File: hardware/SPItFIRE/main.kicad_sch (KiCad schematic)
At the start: 36 parts, among them J1 Compact Host, J10 ISP, J11 Joystick A, J12 Joystick B, J13 Peripheral DE-9, J14 Peripheral User Port, J2 User Port Host, J3 User Port Passthrough, J4 SD Card Adapter, J5 DeadOnRTC, J6 SPI_4, J7 SPI_5, J8 SPI_6, J9 SPI_7, U1 74HC138, U2 ATmega1284P-A, Y1 Crystal

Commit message: Work in progress on layout and routing
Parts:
- C1, C10, C4, C5, C7, C8, C9, R1, R2, R3, R4, R5, R6: footprint (none) -> Capacitor_SMD:C_0603_1608Metric_Pad1.08x0.95mm_HandSolder
- C2, C6: footprint (none) -> Capacitor_SMD:C_0201_0603Metric_Pad0.64x0.40mm_HandSolder
- C3, D2: footprint (none) -> LED_SMD:LED_0603_1608Metric_Pad1.05x0.95mm_HandSolder
- D1: footprint (none) -> Diode_SMD:D_SOD-123
- J10: footprint Package_SO:SOIC-16_3.9x9.9mm_P1.27mm -> Connector_IDC:IDC-Header_2x03_P2.54mm_Vertical
- J14, J2: footprint Connector_PinHeader_2.54mm:PinHeader_2x10_P2.54mm_Horizontal -> Connector_IDC:IDC-Header_2x10_P2.54mm_Latch_Horizontal
- J3: footprint Connector_PinHeader_2.54mm:PinHeader_2x10_P2.54mm_Vertical -> Connector_IDC:IDC-Header_2x10_P2.54mm_Vertical
- L1: footprint (none) -> Inductor_SMD:L_0805_2012Metric_Pad1.05x1.20mm_HandSolder
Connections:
- net AGND is gone; now on net GND: J11.8, J12.8
- net VREF is gone; now on net AVCC: J11.11 (P111), J11.14 (P14), J12.11 (P111), J12.14 (P14)
- net AVCC: now reaches C9.1, L1.2, U2.27 (AVCC)
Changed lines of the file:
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@@
 	)
 	(junction
+		(at 275.59 236.22)
+		(diameter 0)
+		(color 0 0 0 0)
+	)
+	(junction
 		(at 219.71 270.51)
 		(diameter 0)
@@
 	(wire
 		(pts
+			(xy 275.59 236.22) (xy 287.02 236.22)
+		)
+		(stroke
+			(width 0)
+			(type default)
+		)
+	)
+	(wire
+		(pts
 			(xy 284.48 252.73) (xy 287.02 252.73)
 		)
@@
 		)
 	)
+	(label "AVCC"
+		(at 363.22 64.77 0)
+		(effects
+			(font
+				(size 1.27 1.27)
+			)
+			(justify left bottom)
+		)
+	)
 	(global_label "PD2"
 		(shape bidirectional)
@@
 		)
 	)
-	(global_label "VREF"
+	(global_label "AVCC"
 		(shape passive)
 		(at 363.22 114.3 180)
@@
 		)
 		(property "Intersheetrefs" "${INTERSHEET_REFS}"
-			(at 356.7499 114.3 0)
+			(at 356.6289 114.3 0)
 			(hide yes)
 			(show_name no)
@@
 		)
 	)
-	(global_label "VREF"
+	(global_label "AVCC"
 		(shape passive)
 		(at 363.22 129.54 180)
@@
 		)
 		(property "Intersheetrefs" "${INTERSHEET_REFS}"
-			(at 356.7499 129.54 0)
+			(at 356.6289 129.54 0)
 			(hide yes)
 			(show_name no)
@@
 		)
 	)
+	(global_label "AVCC"
+		(shape passive)
+		(at 287.02 236.22 0)
+		(fields_autoplaced yes)
+		(effects
+			(font
+				(size 1.27 1.27)
+			)
+			(justify left)
+		)
+		(property "Intersheetrefs" "${INTERSHEET_REFS}"
+			(at 293.6111 236.22 0)
+			(hide yes)
+			(show_name no)
+			(do_not_autoplace no)
+			(effects
+				(font
+					(size 1.27 1.27)
+				)
+				(justify left)
+			)
+		)
+	)
 	(global_label "PC1"
 		(shape bidirectional)
@@
 		)
 	)
-	(global_label "VREF"
+	(global_label "AVCC"
 		(shape passive)
 		(at 363.22 64.77 180)
@@
 		)
 		(property "Intersheetrefs" "${INTERSHEET_REFS}"
-			(at 356.7499 64.77 0)
+			(at 356.6289 64.77 0)
 			(hide yes)
 			(show_name no)
@@
 		)
 	)
-	(global_label "VREF"
+	(global_label "AVCC"
 		(shape passive)
 		(at 363.22 49.53 180)
@@
 		)
 		(property "Intersheetrefs" "${INTERSHEET_REFS}"
-			(at 356.7499 49.53 0)
+			(at 356.6289 49.53 0)
 			(hide yes)
 			(show_name no)
@@
 		)
 	)
-	(global_label "AGND"
+	(global_label "GND"
 		(shape passive)
 		(at 363.22 72.39 180)
@@
 		)
 		(property "Intersheetrefs" "${INTERSHEET_REFS}"
-			(at 356.387 72.39 0)
+			(at 357.4756 72.39 0)
 			(hide yes)
 			(show_name no)
@@
 		)
 	)
-	(global_label "AGND"
+	(global_label "GND"
 		(shape passive)
 		(at 363.22 137.16 180)
@@
 		)
 		(property "Intersheetrefs" "${INTERSHEET_REFS}"
-			(at 356.387 137.16 0)
+			(at 357.4756 137.16 0)
 			(hide yes)
 			(show_name no)
@@
 			)
 		)
-		(property "Footprint" ""
+		(property "Footprint" "Capacitor_SMD:C_0603_1608Metric_Pad1.08x0.95mm_HandSolder"
 			(at 235.712 186.69 90)
 			(hide yes)
@@
 			)
 		)
-		(property "Footprint" ""
+		(property "Footprint" "Inductor_SMD:L_0805_2012Metric_Pad1.05x1.20mm_HandSolder"
 			(at 256.54 236.22 0)
 			(hide yes)
@@
 			)
 		)
-		(property "Footprint" ""
+		(property "Footprint" "LED_SMD:LED_0603_1608Metric_Pad1.05x0.95mm_HandSolder"
 			(at 237.49 196.85 0)
 			(hide yes)
@@
 			)
 		)
-		(property "Footprint" ""
+		(property "Footprint" "Capacitor_SMD:C_0603_1608Metric_Pad1.08x0.95mm_HandSolder"
 			(at 287.9852 266.7 0)
 			(hide yes)
@@
 			)
 		)
-		(property "Footprint" ""
+		(property "Footprint" "Capacitor_SMD:C_0603_1608Metric_Pad1.08x0.95mm_HandSolder"
 			(at 266.3952 256.54 0)
 			(hide yes)
@@
 			)
 		)
-		(property "Footprint" "Connector_PinHeader_2.54mm:PinHeader_2x10_P2.54mm_Horizontal"
+		(property "Footprint" "Connector_IDC:IDC-Header_2x10_P2.54mm_Latch_Horizontal"
 			(at 25.4 135.89 0)
 			(hide yes)
@@
 			)
 		)
-		(property "Footprint" "Connector_PinHeader_2.54mm:PinHeader_2x10_P2.54mm_Horizontal"
+		(property "Footprint" "Connector_IDC:IDC-Header_2x10_P2.54mm_Latch_Horizontal"
 			(at 374.65 212.09 0)
 			(hide yes)
@@
 			)
 		)
-		(property "Footprint" ""
+		(property "Footprint" "Capacitor_SMD:C_0201_0603Metric_Pad0.64x0.40mm_HandSolder"
 			(at 172.72 171.45 0)
 			(hide yes)
@@
 			)
 		)
-		(property "Footprint" ""
+		(property "Footprint" "Capacitor_SMD:C_0603_1608Metric_Pad1.08x0.95mm_HandSolder"
 			(at 234.6452 256.54 0)
 			(hide yes)
@@
 			)
 		)
-		(property "Footprint" ""
+		(property "Footprint" "Capacitor_SMD:C_0603_1608Metric_Pad1.08x0.95mm_HandSolder"
 			(at 147.0152 45.72 0)
 			(hide yes)
@@
 			)
 		)
-		(property "Footprint" "Connector_PinHeader_2.54mm:PinHeader_2x10_P2.54mm_Vertical"
+		(property "Footprint" "Connector_IDC:IDC-Header_2x10_P2.54mm_Vertical"
 			(at 64.77 135.89 0)
 			(hide yes)
@@
 			)
 		)
-		(property "Footprint" ""
+		(property "Footprint" "Capacitor_SMD:C_0603_1608Metric_Pad1.08x0.95mm_HandSolder"
 			(at 210.5152 256.54 0)
 			(hide yes)
@@
 			)
 		)
-		(property "Footprint" ""
+		(property "Footprint" "Capacitor_SMD:C_0603_1608Metric_Pad1.08x0.95mm_HandSolder"
 			(at 260.35 100.33 0)
 			(hide yes)
@@
 			)
 		)
-		(property "Footprint" ""
+		(property "Footprint" "Capacitor_SMD:C_0603_1608Metric_Pad1.08x0.95mm_HandSolder"
 			(at 257.81 106.68 0)
 			(hide yes)
@@
 			)
 		)
-		(property "Footprint" ""
+		(property "Footprint" "Capacitor_SMD:C_0603_1608Metric_Pad1.08x0.95mm_HandSolder"
 			(at 185.1152 107.95 0)
 			(hide yes)
@@
 			)
 		)
-		(property "Footprint" ""
+		(property "Footprint" "LED_SMD:LED_0603_1608Metric_Pad1.05x0.95mm_HandSolder"
 			(at 174.9552 256.54 0)
 			(hide yes)
@@
 			)
 		)
-		(property "Footprint" ""
+		(property "Footprint" "Diode_SMD:D_SOD-123"
 			(at 179.07 83.82 0)
 			(hide yes)
@@
 			)
 		)
-		(property "Footprint" "Package_SO:SOIC-16_3.9x9.9mm_P1.27mm"
+		(property "Footprint" "Connector_IDC:IDC-Header_2x03_P2.54mm_Vertical"
 			(at 267.97 134.62 0)
 			(hide yes)
@@
 			)
 		)
-		(property "Footprint" ""
+		(property "Footprint" "Capacitor_SMD:C_0603_1608Metric_Pad1.08x0.95mm_HandSolder"
 			(at 252.73 120.65 0)
 			(hide yes)
@@
 			)
 		)
-		(property "Footprint" ""
+		(property "Footprint" "Capacitor_SMD:C_0603_1608Metric_Pad1.08x0.95mm_HandSolder"
 			(at 187.6552 256.54 0)
 			(hide yes)
@@
 			)
 		)
-		(property "Footprint" ""
+		(property "Footprint" "Capacitor_SMD:C_0201_0603Metric_Pad0.64x0.40mm_HandSolder"
 			(at 187.96 171.45 0)
 			(hide yes)
@@
 			)
 		)
-		(property "Footprint" ""
+		(property "Footprint" "Capacitor_SMD:C_0603_1608Metric_Pad1.08x0.95mm_HandSolder"
 			(at 187.452 83.82 90)
 			(hide yes)
@@
 			)
 		)
-		(property "Footprint" ""
+		(property "Footprint" "Capacitor_SMD:C_0603_1608Metric_Pad1.08x0.95mm_HandSolder"
 			(at 255.27 114.3 0)
 			(hide yes)

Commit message: Completed layout and routing. Now need to work through the few DRC errors
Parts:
- added H301, H302, H303, H304, H305, H306, H307, H308: MountingHole_Pad, MountingHole:MountingHole_2.2mm_M2_DIN965_Pad, symbol Mechanical:MountingHole_Pad
- J1: symbol Connector:DE9_Socket -> Connector:DE9_Socket_MountingHoles
- J11, J12: symbol Connector:DA15_Socket -> Connector:DA15_Socket_MountingHoles
- J13: symbol Connector:DE9_Pins -> Connector:DE9_Pins_MountingHoles
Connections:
- net GND: now also J1.SH (PAD), J11.SH (PAD), J12.SH (PAD), J13.SH (PAD), H301.1, H302.1, H303.1, H304.1, H305.1, H306.1, H307.1, H308.1

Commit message: Added BoM
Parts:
- C2, C6: value C_Small -> pF
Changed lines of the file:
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@@
 			)
 		)
-		(property "Value" "C_Small"
+		(property "Value" "pF"
 			(at 163.068 173.228 0)
 			(show_name no)
@@
 			)
 		)
-		(property "Value" "C_Small"
+		(property "Value" "pF"
 			(at 190.5 172.7262 0)
 			(show_name no)

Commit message: Use updated footprints from the SPItFIRE library
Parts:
- added R7: 10K, Resistor_SMD:R_0603_1608Metric_Pad0.98x0.95mm_HandSolder, symbol Device:R
- C2, C6: value pF -> 27pF
- J14, J2: footprint Connector_IDC:IDC-Header_2x10_P2.54mm_Latch_Horizontal -> SPItFIRE:IDC-Header_2x10_P2.54mm_Latch_Horizontal
- R1, R2, R3, R4, R5, R6: footprint Capacitor_SMD:C_0603_1608Metric_Pad1.08x0.95mm_HandSolder -> Resistor_SMD:R_0603_1608Metric_Pad0.98x0.95mm_HandSolder
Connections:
- net +5V: now also R7.1
- net MISO: now also R7.2
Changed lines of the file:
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@@
 	)
 	(junction
+		(at 111.76 96.52)
+		(diameter 0)
+		(color 0 0 0 0)
+	)
+	(junction
 		(at 107.95 210.82)
 		(diameter 0)
@@
 	)
 	(junction
+		(at 95.25 77.47)
+		(diameter 0)
+		(color 0 0 0 0)
+	)
+	(junction
 		(at 39.37 99.06)
 		(diameter 0)
@@
 	)
 	(junction
-		(at 41.91 96.52)
-		(diameter 0)
-		(color 0 0 0 0)
-	)
-	(junction
 		(at 96.52 167.64)
 		(diameter 0)
@@
 	)
 	(junction
+		(at 41.91 96.52)
+		(diameter 0)
+		(color 0 0 0 0)
+	)
+	(junction
 		(at 172.72 165.1)
 		(diameter 0)
@@
 	(wire
 		(pts
+			(xy 111.76 96.52) (xy 116.84 96.52)
+		)
+		(stroke
+			(width 0)
+			(type default)
+		)
+	)
+	(wire
+		(pts
 			(xy 388.62 222.25) (xy 388.62 224.79)
 		)
@@
 	(wire
 		(pts
-			(xy 41.91 96.52) (xy 95.25 96.52)
+			(xy 41.91 96.52) (xy 111.76 96.52)
 		)
 		(stroke
@@
 	(wire
 		(pts
+			(xy 111.76 90.17) (xy 111.76 96.52)
+		)
+		(stroke
+			(width 0)
+			(type default)
+		)
+	)
+	(wire
+		(pts
 			(xy 363.22 41.91) (xy 367.03 41.91)
 		)
@@
 	(wire
 		(pts
+			(xy 95.25 77.47) (xy 111.76 77.47)
+		)
+		(stroke
+			(width 0)
+			(type default)
+		)
+	)
+	(wire
+		(pts
 			(xy 257.81 92.71) (xy 257.81 104.14)
 		)
@@
 	(wire
 		(pts
+			(xy 111.76 77.47) (xy 111.76 82.55)
+		)
+		(stroke
+			(width 0)
+			(type default)
+		)
+	)
+	(wire
+		(pts
 			(xy 17.78 146.05) (xy 20.32 146.05)
 		)
@@
 	(global_label "MISO"
 		(shape input)
-		(at 95.25 96.52 0)
+		(at 116.84 96.52 0)
 		(fields_autoplaced yes)
 		(effects
@@
 		)
 		(property "Intersheetrefs" "${INTERSHEET_REFS}"
-			(at 102.8314 96.52 0)
+			(at 124.4214 96.52 0)
 			(hide yes)
 			(show_name no)
@@
 			)
 		)
-		(property "Footprint" "Capacitor_SMD:C_0603_1608Metric_Pad1.08x0.95mm_HandSolder"
+		(property "Footprint" "Resistor_SMD:R_0603_1608Metric_Pad0.98x0.95mm_HandSolder"
 			(at 235.712 186.69 90)
 			(hide yes)
@@
 			)
 		)
-		(property "Footprint" "Connector_IDC:IDC-Header_2x10_P2.54mm_Latch_Horizontal"
+		(property "Footprint" "SPItFIRE:IDC-Header_2x10_P2.54mm_Latch_Horizontal"
 			(at 25.4 135.89 0)
 			(hide yes)
@@
 			)
 		)
-		(property "Footprint" "Connector_IDC:IDC-Header_2x10_P2.54mm_Latch_Horizontal"
+		(property "Footprint" "SPItFIRE:IDC-Header_2x10_P2.54mm_Latch_Horizontal"
 			(at 374.65 212.09 0)
 			(hide yes)
@@
 			)
 		)
-		(property "Value" "pF"
-			(at 163.068 173.228 0)
+		(property "Value" "27pF"
+			(at 165.608 172.212 0)
 			(show_name no)
 			(do_not_autoplace no)
@@
 			)
 		)
-		(property "Footprint" "Capacitor_SMD:C_0603_1608Metric_Pad1.08x0.95mm_HandSolder"
+		(property "Footprint" "Resistor_SMD:R_0603_1608Metric_Pad0.98x0.95mm_HandSolder"
 			(at 260.35 100.33 0)
 			(hide yes)
@@
 			)
 		)
-		(property "Footprint" "Capacitor_SMD:C_0603_1608Metric_Pad1.08x0.95mm_HandSolder"
+		(property "Footprint" "Resistor_SMD:R_0603_1608Metric_Pad0.98x0.95mm_HandSolder"
 			(at 257.81 106.68 0)
 			(hide yes)
@@
 			)
 		)
-		(property "Footprint" "Capacitor_SMD:C_0603_1608Metric_Pad1.08x0.95mm_HandSolder"
+		(property "Footprint" "Resistor_SMD:R_0603_1608Metric_Pad0.98x0.95mm_HandSolder"
 			(at 252.73 120.65 0)
 			(hide yes)
@@
 	)
 	(symbol
+		(lib_id "Device:R")
+		(at 111.76 86.36 0)
+		(unit 1)
+		(body_style 1)
+		(exclude_from_sim no)
+		(in_bom yes)
+		(on_board yes)
+		(in_pos_files yes)
+		(dnp no)
+		(fields_autoplaced yes)
+		(property "Reference" "R7"
+			(at 114.3 85.0899 0)
+			(show_name no)
+			(do_not_autoplace no)
+			(effects
+				(font
+					(size 1.27 1.27)
+				)
+				(justify left)
+			)
+		)
+		(property "Value" "10K"
+			(at 114.3 87.6299 0)
+			(show_name no)
+			(do_not_autoplace no)
+			(effects
+				(font
+					(size 1.27 1.27)
+				)
+				(justify left)
+			)
+		)
+		(property "Footprint" "Resistor_SMD:R_0603_1608Metric_Pad0.98x0.95mm_HandSolder"
+			(at 109.982 86.36 90)
+			(hide yes)
+			(show_name no)
+			(do_not_autoplace no)
+			(effects
+				(font
+					(size 1.27 1.27)
+				)
+			)
+		)
+		(property "Datasheet" ""
+			(at 111.76 86.36 0)
+			(hide yes)
+			(show_name no)
+			(do_not_autoplace no)
+			(effects
+				(font
+					(size 1.27 1.27)
+				)
+			)
+		)
+		(property "Description" "Resistor"
+			(at 111.76 86.36 0)
+			(hide yes)
+			(show_name no)
+			(do_not_autoplace no)
+			(effects
+				(font
+					(size 1.27 1.27)
+				)
+			)
+		)
+		(pin "2"
+		)
+		(pin "1"
+		)
+		(instances
+			(project "SPItFIRE"
+				(path "/148e0ceb-efca-48fe-9d35-9803ba402dc8/66bc930e-1178-4e6f-bc8c-4ce2829b38df"
+					(reference "R7")
+					(unit 1)
+				)
+			)
+		)
+	)
+	(symbol
 		(lib_id "Mechanical:MountingHole_Pad")
 		(at 154.94 144.78 0)
@@
 			)
 		)
-		(property "Value" "pF"
+		(property "Value" "27pF"
 			(at 190.5 172.7262 0)
 			(show_name no)
@@
 			)
 		)
-		(property "Footprint" "Capacitor_SMD:C_0603_1608Metric_Pad1.08x0.95mm_HandSolder"
+		(property "Footprint" "Resistor_SMD:R_0603_1608Metric_Pad0.98x0.95mm_HandSolder"
 			(at 187.452 83.82 90)
 			(hide yes)
@@
 			)
 		)
-		(property "Footprint" "Capacitor_SMD:C_0603_1608Metric_Pad1.08x0.95mm_HandSolder"
+		(property "Footprint" "Resistor_SMD:R_0603_1608Metric_Pad0.98x0.95mm_HandSolder"
 			(at 255.27 114.3 0)
 			(hide yes)

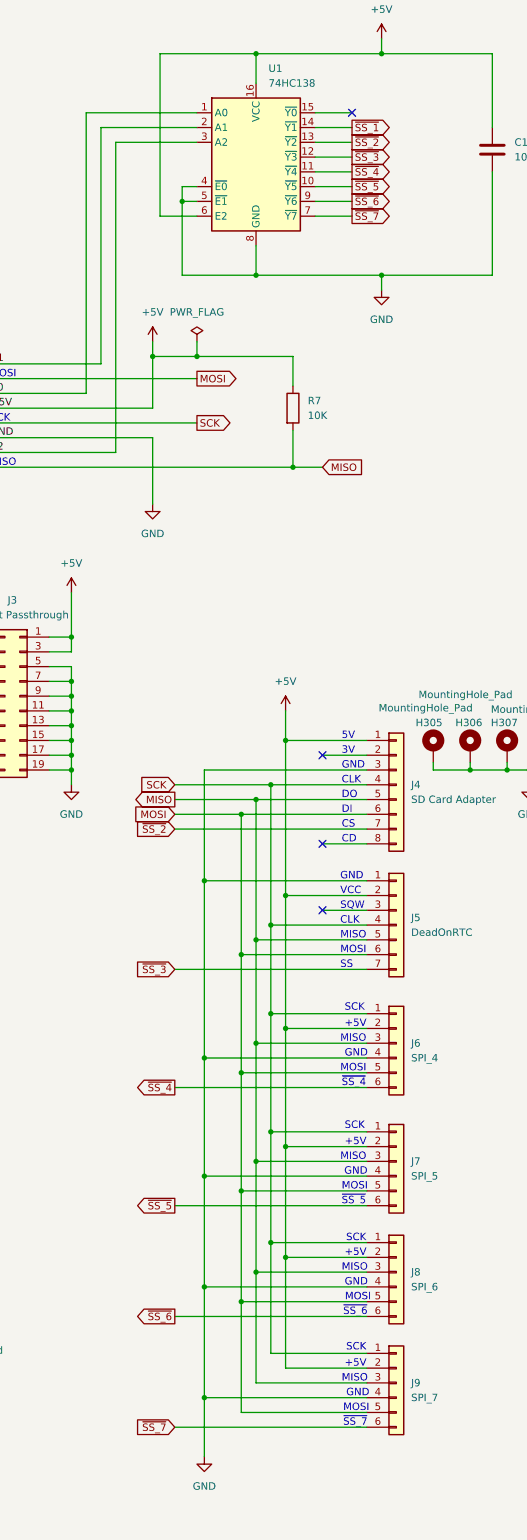
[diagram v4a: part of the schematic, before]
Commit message: Reallocate the decoder outputs: Y7 is "no device"
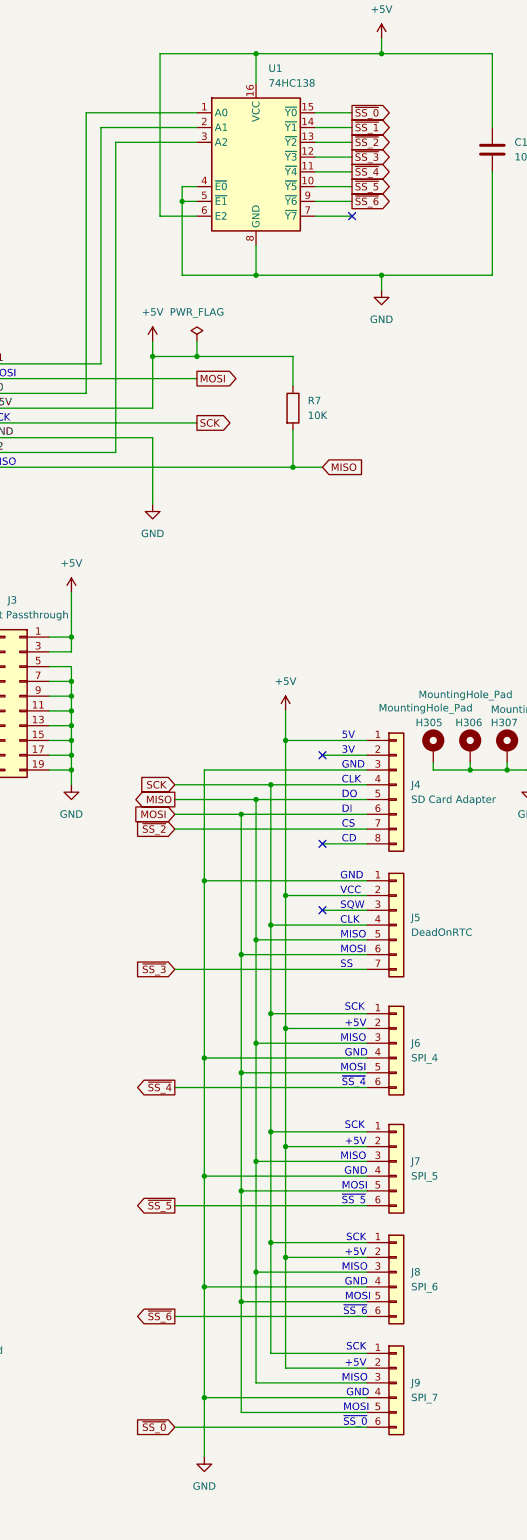
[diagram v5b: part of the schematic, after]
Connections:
- net ~{SS_0}: now reaches U1.15 (~{Y0})
- net ~{SS_0}: now also J9.6 (Pin_6)
- net ~{SS_7}: no longer names the net of U1.7 (~{Y7})
- net ~{SS_7}: no longer J9.6 (Pin_6)
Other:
- note added: "~{SS_0}"
- note removed: "~{SS_7}"
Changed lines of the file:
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@@
 		)
 	)
-	(text "~{SS_7}"
+	(text "~{SS_0}"
 		(exclude_from_sim no)
 		(at 120.396 260.858 0)
@@
 	)
 	(no_connect
-		(at 121.92 35.56)
+		(at 363.22 104.14)
 	)
 	(no_connect
-		(at 363.22 104.14)
+		(at 121.92 53.34)
 	)
 	(no_connect
@@
 		)
 	)
-	(global_label "~{SS_7}"
-		(shape output)
-		(at 121.92 53.34 0)
-		(fields_autoplaced yes)
-		(effects
-			(font
-				(size 1.27 1.27)
-			)
-			(justify left)
-		)
-		(property "Intersheetrefs" "${INTERSHEET_REFS}"
-			(at 129.5013 53.34 0)
-			(hide yes)
-			(show_name no)
-			(do_not_autoplace no)
-			(effects
-				(font
-					(size 1.27 1.27)
-				)
-				(justify left)
-			)
-		)
-	)
 	(global_label "SCK"
 		(shape output)
@@
 		)
 	)
-	(global_label "~{SS_7}"
+	(global_label "~{SS_0}"
 		(shape input)
 		(at 91.44 261.62 180)
@@
 			(hide yes)
 			(show_name no)
+			(do_not_autoplace no)
+			(effects
+				(font
+					(size 1.27 1.27)
+				)
+				(justify left)
+			)
+		)
+	)
+	(global_label "~{SS_0}"
+		(shape output)
+		(at 121.92 35.56 0)
+		(fields_autoplaced yes)
+		(effects
+			(font
+				(size 1.27 1.27)
+			)
+			(justify left)
+		)
+		(property "Intersheetrefs" "${INTERSHEET_REFS}"
+			(at 129.5013 35.56 0)
+			(hide yes)
+			(show_name no)
